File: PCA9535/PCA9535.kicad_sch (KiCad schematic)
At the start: 14 parts, among them J1 Conn_01x04, J2 Conn_01x04, J3 Conn_02x05_Odd_Even, J4 Conn_01x01, J5 Conn_01x10, J6 Conn_02x05_Odd_Even, U1 PCA9535DBR

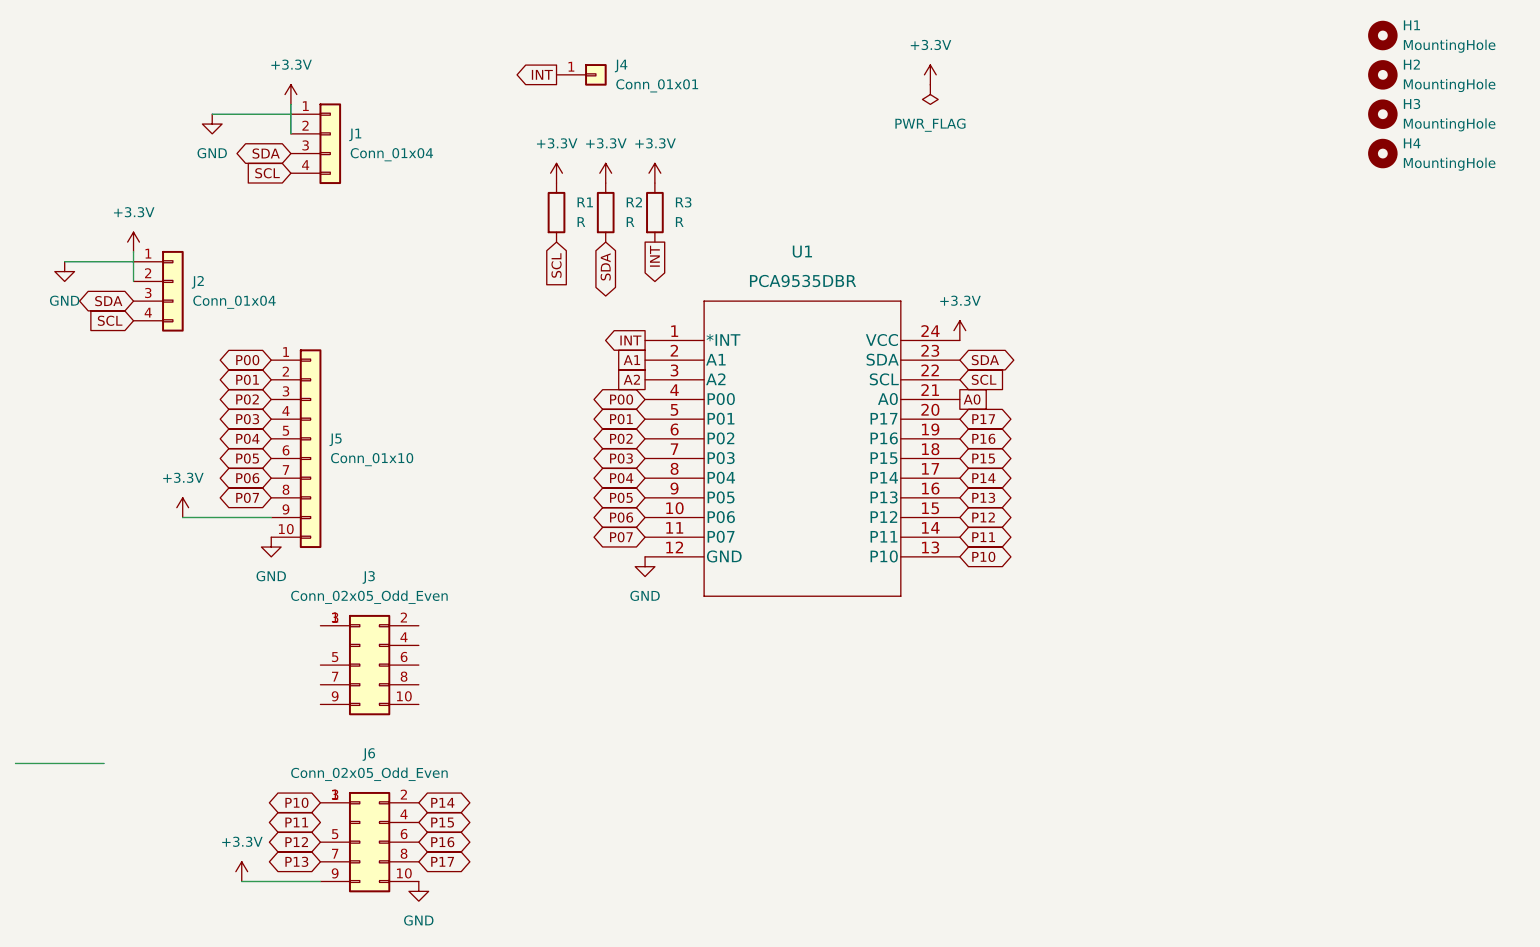
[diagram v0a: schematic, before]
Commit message: Updating GPIO expansion board
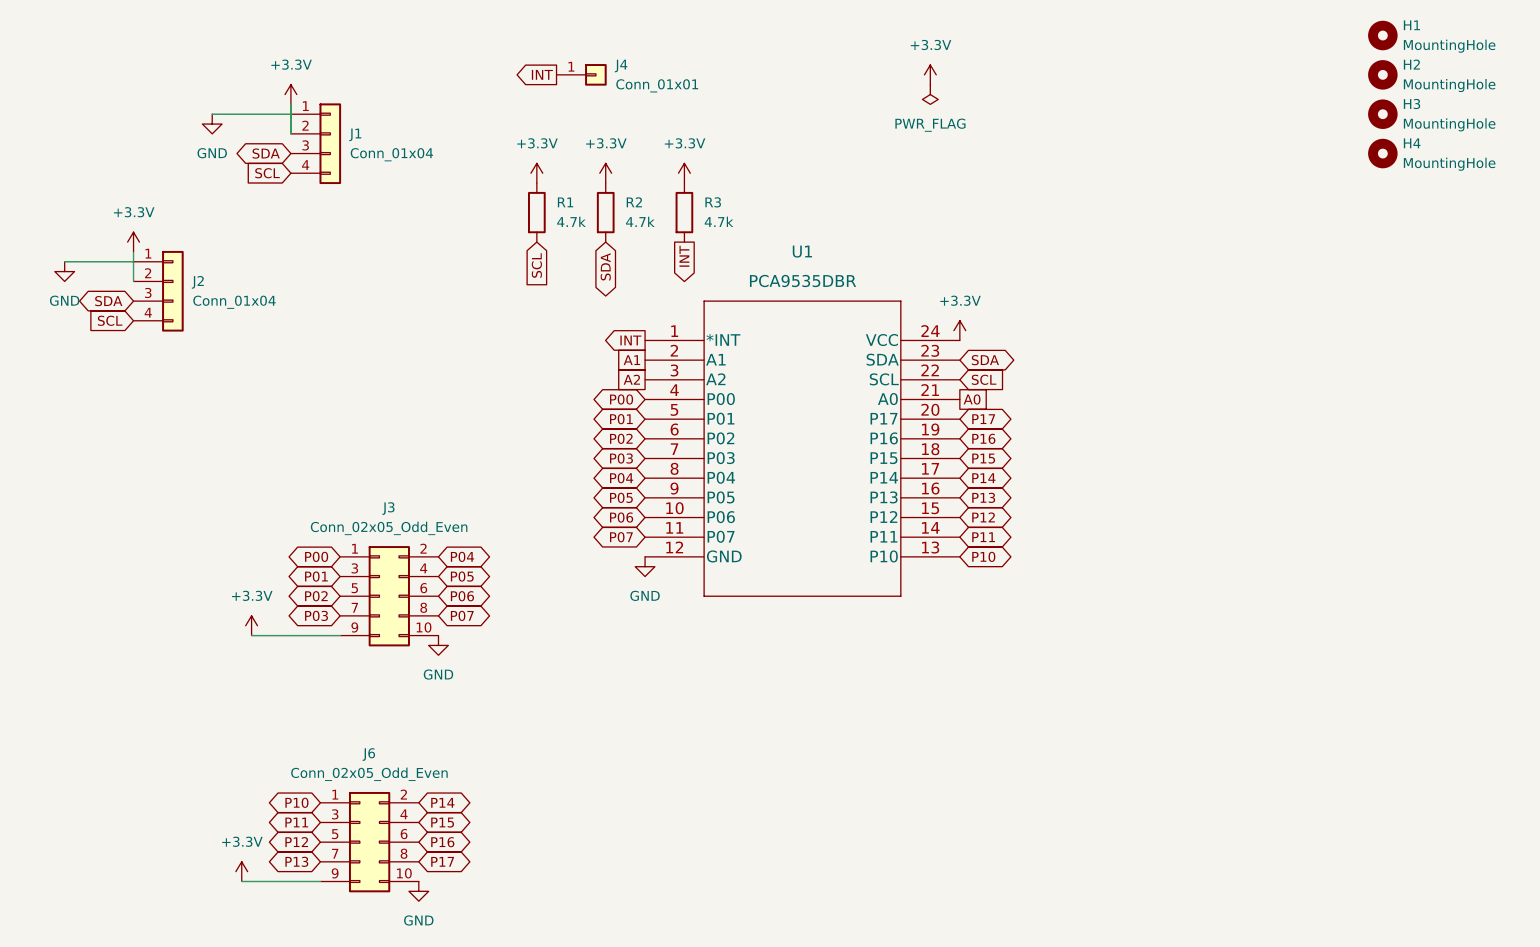
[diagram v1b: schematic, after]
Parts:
- removed J5: Conn_01x10, Connector_PinHeader_2.54mm:PinHeader_1x10_P2.54mm_Vertical, symbol Connector_Generic:Conn_01x10
- J3, J6: footprint (none) -> Connector_PinHeader_2.54mm:PinHeader_2x05_P2.54mm_Vertical
- R1, R2, R3: value R -> 4.7k
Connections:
- net +3.3V: now also J3.9 (Pin_9)
- net GND: now also J3.10 (Pin_10)
- net P00: now also J3.1 (Pin_1)
- net P01: now also J3.3 (Pin_3)
- net P02: now also J3.5 (Pin_5)
- net P03: now also J3.7 (Pin_7)
- net P04: now also J3.2 (Pin_2)
- net P05: now also J3.4 (Pin_4)
- net P06: now also J3.6 (Pin_6)
- net P07: now also J3.8 (Pin_8)
- net P10: no longer J6.3 (Pin_3)
- net P11: now also J6.3 (Pin_3)
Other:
- moved on the sheet: R1, R3

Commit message: Figured out solder jumpers, kinda
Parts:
- added JP1, JP2, JP3: SolderJumper_3_Open, Jumper:SolderJumper-3_P1.3mm_Open_Pad1.0x1.5mm, symbol Jumper:SolderJumper_3_Open
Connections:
- net +3.3V: now also JP1.1 (A), JP2.1 (A), JP3.1 (A)
- net A0: now also JP1.2 (C)
- net A1: now also JP2.2 (C)
- net A2: now also JP3.2 (C)
- net GND: now also JP1.3 (B), JP2.3 (B), JP3.3 (B)
